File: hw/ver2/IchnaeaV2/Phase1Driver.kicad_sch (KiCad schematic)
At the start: 21 parts, among them Q2 MCAC80N10Y, Q3 MCAC80N10Y, Q4 MCAC80N10Y, Q5 MCAC80N10Y, U2 HIP2210

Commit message: Trying to optimize the high power loop area
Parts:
- renumbered C6 to C18, C7 to C19, C8 to C20, C9 to C21, C10 to C22, C11 to C23, C42 to C44, C48 to C50, C54 to C56, C60 to C62, D2 to D4, L1 to L3, Q2 to Q10, Q3 to Q11, Q4 to Q12, Q5 to Q13, R4 to R12, R5 to R13, R6 to R14, R7 to R15, U2 to U4
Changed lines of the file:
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@@
 		(on_board yes)
 		(dnp no)
-		(property "Reference" "R5"
+		(property "Reference" "R13"
 			(at 123.19 100.584 90)
 			(effects
@@
 		(on_board yes)
 		(dnp no)
-		(property "Reference" "C9"
+		(property "Reference" "C21"
 			(at 191.77 71.1199 0)
 			(effects
@@
 		(dnp no)
 		(fields_autoplaced yes)
-		(property "Reference" "C48"
+		(property "Reference" "C50"
 			(at 242.57 100.3299 0)
 			(effects
@@
 		(on_board yes)
 		(dnp no)
-		(property "Reference" "L1"
+		(property "Reference" "L3"
 			(at 203.2 92.456 90)
 			(effects
@@
 		(on_board yes)
 		(dnp no)
-		(property "Reference" "C6"
+		(property "Reference" "C18"
 			(at 87.63 95.2499 0)
 			(effects
@@
 		(dnp no)
 		(fields_autoplaced yes)
-		(property "Reference" "#PWR068"
+		(property "Reference" "#PWR070"
 			(at 227.33 111.76 0)
 			(effects
@@
 		(dnp no)
 		(fields_autoplaced yes)
-		(property "Reference" "#PWR045"
+		(property "Reference" "#PWR053"
 			(at 127 113.03 0)
 			(effects
@@
 		(dnp no)
 		(fields_autoplaced yes)
-		(property "Reference" "#PWR086"
+		(property "Reference" "#PWR088"
 			(at 261.62 111.76 0)
 			(effects
@@
 		(dnp no)
 		(fields_autoplaced yes)
-		(property "Reference" "R7"
+		(property "Reference" "R15"
 			(at 207.01 76.1999 0)
 			(effects
@@
 		(on_board yes)
 		(dnp no)
-		(property "Reference" "Q3"
+		(property "Reference" "Q11"
 			(at 153.924 109.22 0)
 			(effects
@@
 		(dnp no)
 		(fields_autoplaced yes)
-		(property "Reference" "C42"
+		(property "Reference" "C44"
 			(at 231.14 100.3299 0)
 			(effects
@@
 		(on_board yes)
 		(dnp no)
-		(property "Reference" "R4"
+		(property "Reference" "R12"
 			(at 111.76 86.868 90)
 			(effects
@@
 		(on_board yes)
 		(dnp no)
-		(property "Reference" "Q2"
+		(property "Reference" "Q10"
 			(at 155.956 79.502 0)
 			(effects
@@
 		(dnp no)
 		(fields_autoplaced yes)
-		(property "Reference" "C11"
+		(property "Reference" "C23"
 			(at 219.71 100.3299 0)
 			(effects
@@
 		(on_board yes)
 		(dnp no)
-		(property "Reference" "C8"
+		(property "Reference" "C20"
 			(at 145.796 84.328 0)
 			(effects
@@
 		(dnp no)
 		(fields_autoplaced yes)
-		(property "Reference" "#PWR080"
+		(property "Reference" "#PWR082"
 			(at 250.19 111.76 0)
 			(effects
@@
 		(dnp no)
 		(fields_autoplaced yes)
-		(property "Reference" "C10"
+		(property "Reference" "C22"
 			(at 208.28 66.0399 0)
 			(effects
@@
 		(dnp no)
 		(fields_autoplaced yes)
-		(property "Reference" "#PWR047"
+		(property "Reference" "#PWR055"
 			(at 215.9 111.76 0)
 			(effects
@@
 		(on_board yes)
 		(dnp no)
-		(property "Reference" "C7"
+		(property "Reference" "C19"
 			(at 101.6 95.2499 0)
 			(effects
@@
 		(on_board yes)
 		(dnp no)
-		(property "Reference" "Q4"
+		(property "Reference" "Q12"
 			(at 168.656 79.756 0)
 			(effects
@@
 		(dnp no)
 		(fields_autoplaced yes)
-		(property "Reference" "R6"
+		(property "Reference" "R14"
 			(at 190.5 76.2 90)
 			(effects
@@
 		(dnp no)
 		(fields_autoplaced yes)
-		(property "Reference" "#PWR074"
+		(property "Reference" "#PWR076"
 			(at 238.76 111.76 0)
 			(effects
@@
 		(on_board yes)
 		(dnp no)
-		(property "Reference" "Q5"
+		(property "Reference" "Q13"
 			(at 168.148 109.22 0)
 			(effects
@@
 		(on_board yes)
 		(dnp no)
-		(property "Reference" "D2"
+		(property "Reference" "D4"
 			(at 114.3 95.2499 90)
 			(effects
@@
 		(dnp no)
 		(fields_autoplaced yes)
-		(property "Reference" "C54"
+		(property "Reference" "C56"
 			(at 254 100.3299 0)
 			(effects
@@
 		(dnp no)
 		(fields_autoplaced yes)
-		(property "Reference" "#PWR044"
+		(property "Reference" "#PWR052"
 			(at 105.41 109.22 0)
 			(effects
@@
 		(dnp no)
 		(fields_autoplaced yes)
-		(property "Reference" "#PWR046"
+		(property "Reference" "#PWR054"
 			(at 162.56 113.03 0)
 			(effects
@@
 		(dnp no)
 		(fields_autoplaced yes)
-		(property "Reference" "C60"
+		(property "Reference" "C62"
 			(at 265.43 100.3299 0)
 			(effects
@@
 		(dnp no)
 		(fields_autoplaced yes)
-		(property "Reference" "U2"
+		(property "Reference" "U4"
 			(at 135.89 78.74 0)
 			(effects

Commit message: Trying to further compress power loop area
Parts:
- renumbered C22 to C10, C23 to C11, C44 to C42, C50 to C48, C56 to C54, C18 to C6, C62 to C60, C19 to C7, C20 to C8, C21 to C9, D4 to D2, L3 to L1, Q10 to Q2, Q11 to Q3, Q12 to Q4, Q13 to Q5, R12 to R4, R13 to R5, R14 to R6, R15 to R7, U4 to U2

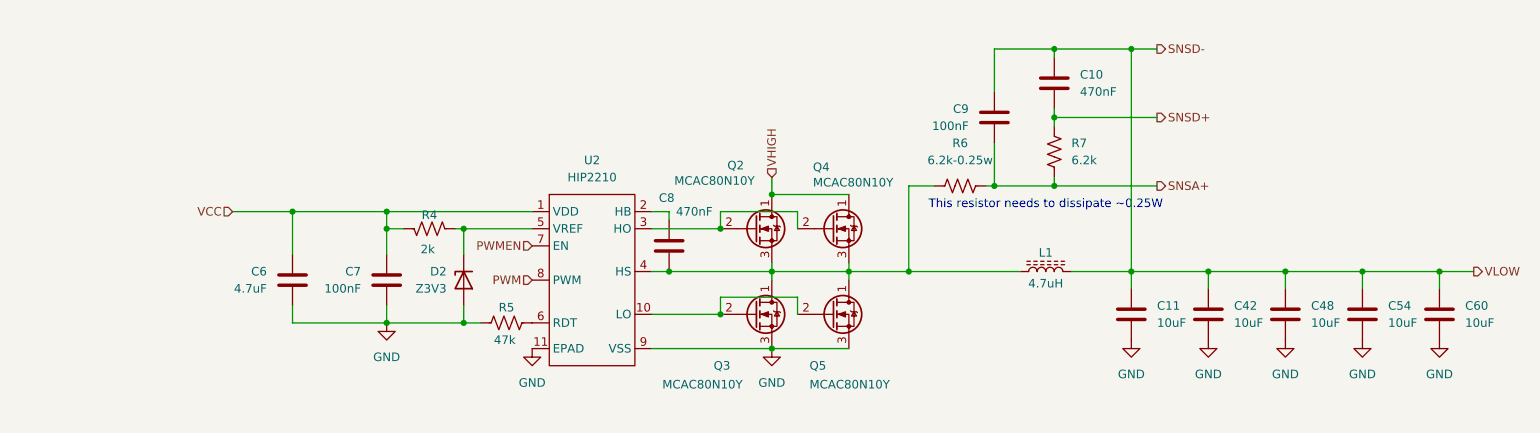
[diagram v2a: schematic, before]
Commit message: Not quite happy with the power stage just yet.
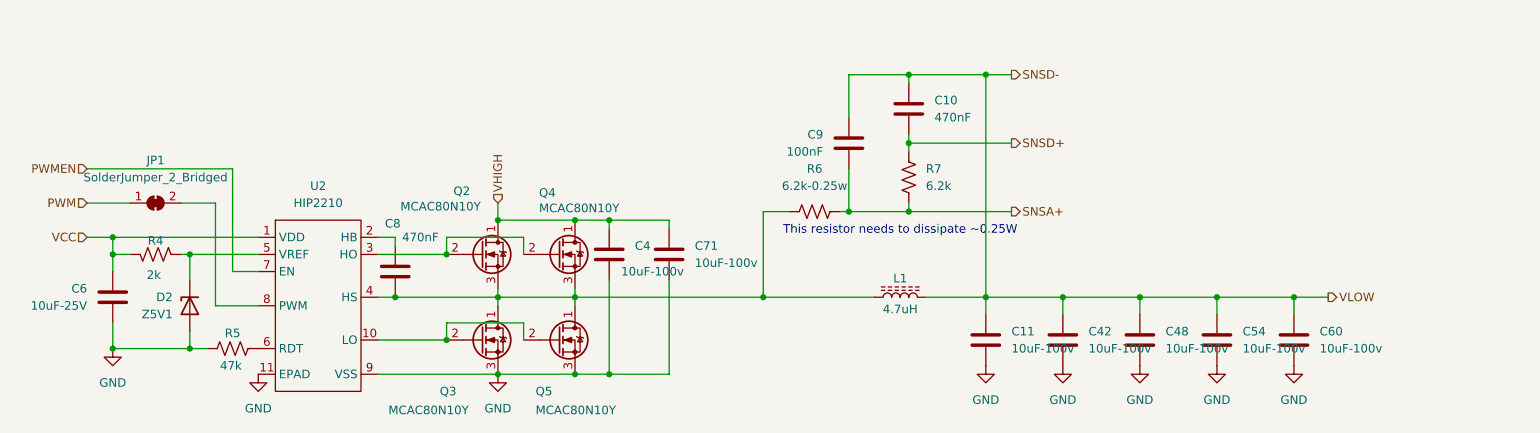
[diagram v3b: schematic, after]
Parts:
- removed C7: 100nF, Capacitor_SMD:C_0603_1608Metric, symbol Device:C
- added C4, C71: 10uF-100v, Capacitor_SMD:C_1210_3225Metric_Pad1.33x2.70mm_HandSolder, symbol Device:C
- added JP1: SolderJumper_2_Bridged, Jumper:SolderJumper-2_P1.3mm_Bridged_Pad1.0x1.5mm, symbol Jumper:SolderJumper_2_Bridged
- C11, C42, C48, C54, C60: value 10uF -> 10uF-100v
- C6: value 4.7uF -> 10uF-25V; LCSC C19666 -> C96446
- D2: value Z3V3 -> Z5V1; LCSC C5353025 -> C2903912
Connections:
- net GND: now also C4.2, C71.2
- net PWM: now also JP1.1 (A); no longer U2.8 (PWM)
- net VHIGH: now also C4.1, C71.1
- new net: JP1.2 (B), U2.8 (PWM)
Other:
- moved on the sheet: C10, C11, C42, C48, C54, C6, C60, C8, C9, D2, L1, Q2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

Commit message: Sync work to main PC
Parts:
- removed D2: Z5V1, Diode_SMD:D_SOD-123, symbol Device:D_Zener
- removed JP1: SolderJumper_2_Bridged, Jumper:SolderJumper-2_P1.3mm_Bridged_Pad1.0x1.5mm, symbol Jumper:SolderJumper_2_Bridged
- added R74: 0, Resistor_SMD:R_0603_1608Metric, symbol Device:R_US
- added R75: 10k, Resistor_SMD:R_0603_1608Metric, symbol Device:R_US
- added R76: 6.2k, Resistor_SMD:R_0603_1608Metric, symbol Device:R_US
- R4: value 2k -> 0; LCSC (none) -> C21189
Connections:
- net GND: now also R76.2
- net PWM: now also R74.2
- net PWMEN: now also R4.2; no longer U2.7 (EN)
- net SNSD-: now also L1.1; no longer L1.2
- net VCC: now also R75.1; no longer R4.2
- net at C8.2, Q2.3 (S), Q3.1 (D)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: now also L1.2; no longer L1.1
- net at U2.5 (VREF): now also R75.2, R76.1; no longer R4.1
- net at U2.8 (PWM): now also R74.1
- new net: R4.1, U2.7 (EN)
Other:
- moved on the sheet: L1

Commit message: More power stage layout
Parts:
- added TP10, TP11, TP12, TP13, TP6, TP7, TP8, TP9: TestPoint, TestPoint:TestPoint_Pad_D1.0mm, symbol Connector:TestPoint
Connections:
- net GND: now also TP10.1
- net PWM: now also TP7.1
- net PWMEN: now also TP6.1
- net SNSA+: now also TP13.1
- net SNSD+: now also TP12.1
- net SNSD-: now also TP11.1
- net at Q3.2 (G), Q5.2 (G), U2.10 (LO): now also TP8.1
- net at Q2.2 (G), Q4.2 (G), U2.3 (HO): now also TP9.1

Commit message: Partially work through the V1 notes. Start adding some of the control stage circuitry.
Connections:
- net GND: now also TP12.1
- net SNSA+: no longer TP13.1
- net SNSD+: no longer TP12.1
- net at C8.2, L1.2, Q2.3 (S)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: now also TP13.1
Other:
- moved on the sheet: TP11, TP12, TP13
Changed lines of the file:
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@@
 	)
 	(junction
-		(at 217.17 99.06)
+		(at 161.29 86.36)
 		(diameter 0)
 		(color 0 0 0 0)
 	)
 	(junction
-		(at 76.2 92.71)
+		(at 217.17 99.06)
 		(diameter 0)
 		(color 0 0 0 0)
 	)
 	(junction
-		(at 195.58 66.04)
+		(at 76.2 92.71)
 		(diameter 0)
 		(color 0 0 0 0)
@@
 	)
 	(junction
-		(at 195.58 76.2)
-		(diameter 0)
-		(color 0 0 0 0)
-	)
-	(junction
 		(at 205.74 99.06)
 		(diameter 0)
@@
 	)
 	(junction
-		(at 195.58 86.36)
-		(diameter 0)
-		(color 0 0 0 0)
-	)
-	(junction
 		(at 194.31 99.06)
 		(diameter 0)
@@
 	(wire
 		(pts
-			(xy 195.58 86.36) (xy 198.12 86.36)
-		)
-		(stroke
-			(width 0)
-			(type default)
-		)
-	)
-	(wire
-		(pts
 			(xy 111.76 113.03) (xy 113.03 113.03)
 		)
@@
 	(wire
 		(pts
-			(xy 182.88 86.36) (xy 195.58 86.36)
+			(xy 182.88 86.36) (xy 198.12 86.36)
 		)
 		(stroke
@@
 	(wire
 		(pts
-			(xy 195.58 73.66) (xy 195.58 76.2)
-		)
-		(stroke
-			(width 0)
-			(type default)
-		)
-	)
-	(wire
-		(pts
 			(xy 125.73 90.17) (xy 114.3 90.17)
 		)
@@
 	(wire
 		(pts
-			(xy 195.58 66.04) (xy 194.31 66.04)
+			(xy 194.31 66.04) (xy 198.12 66.04)
 		)
 		(stroke
@@
 	(wire
 		(pts
-			(xy 198.12 66.04) (xy 195.58 66.04)
-		)
-		(stroke
-			(width 0)
-			(type default)
-		)
-	)
-	(wire
-		(pts
 			(xy 185.42 99.06) (xy 194.31 99.06)
 		)
@@
 	(wire
 		(pts
-			(xy 195.58 76.2) (xy 198.12 76.2)
-		)
-		(stroke
-			(width 0)
-			(type default)
-		)
-	)
-	(wire
-		(pts
 			(xy 172.72 86.36) (xy 173.99 86.36)
 		)
@@
 	(wire
 		(pts
-			(xy 182.88 76.2) (xy 195.58 76.2)
+			(xy 182.88 76.2) (xy 198.12 76.2)
 		)
 		(stroke
@@
 	(wire
 		(pts
-			(xy 195.58 83.82) (xy 195.58 86.36)
-		)
-		(stroke
-			(width 0)
-			(type default)
-		)
-	)
-	(wire
-		(pts
 			(xy 76.2 92.71) (xy 86.36 92.71)
 		)
@@
 		)
 	)
-	(wire
-		(pts
-			(xy 195.58 63.5) (xy 195.58 66.04)
-		)
-		(stroke
-			(width 0)
-			(type default)
-		)
-	)
 	(text "This resistor needs to dissipate ~0.25W"
 		(exclude_from_sim no)
@@
 	(symbol
 		(lib_id "Connector:TestPoint")
-		(at 195.58 83.82 270)
+		(at 161.29 86.36 0)
 		(unit 1)
 		(exclude_from_sim no)
@@
 		(dnp no)
 		(property "Reference" "TP13"
-			(at 201.93 83.82 90)
+			(at 161.29 80.01 90)
 			(effects
 				(font
@@
 		)
 		(property "Value" "TestPoint"
-			(at 198.882 86.36 90)
+			(at 163.83 83.058 90)
 			(effects
 				(font
@@
 		)
 		(property "Footprint" "TestPoint:TestPoint_Pad_D1.0mm"
-			(at 195.58 88.9 0)
+			(at 166.37 86.36 0)
 			(effects
 				(font
@@
 		)
 		(property "Datasheet" "~"
-			(at 195.58 88.9 0)
+			(at 166.37 86.36 0)
 			(effects
 				(font
@@
 		)
 		(property "Description" "test point"
-			(at 195.58 83.82 0)
+			(at 161.29 86.36 0)
 			(effects
 				(font
@@
 	(symbol
 		(lib_id "Connector:TestPoint")
-		(at 195.58 63.5 270)
+		(at 194.31 66.04 0)
 		(unit 1)
 		(exclude_from_sim no)
@@
 		(dnp no)
 		(property "Reference" "TP11"
-			(at 201.93 63.5 90)
+			(at 194.31 59.69 90)
 			(effects
 				(font
@@
 		)
 		(property "Value" "TestPoint"
-			(at 198.882 66.04 90)
+			(at 196.85 62.738 90)
 			(effects
 				(font
@@
 		)
 		(property "Footprint" "TestPoint:TestPoint_Pad_D1.0mm"
-			(at 195.58 68.58 0)
+			(at 199.39 66.04 0)
 			(effects
 				(font
@@
 		)
 		(property "Datasheet" "~"
-			(at 195.58 68.58 0)
+			(at 199.39 66.04 0)
 			(effects
 				(font
@@
 		)
 		(property "Description" "test point"
-			(at 195.58 63.5 0)
+			(at 194.31 66.04 0)
 			(effects
 				(font
@@
 	(symbol
 		(lib_id "power:GND")
+		(at 158.75 86.36 0)
+		(unit 1)
+		(exclude_from_sim no)
+		(in_bom yes)
+		(on_board yes)
+		(dnp no)
+		(fields_autoplaced yes)
+		(property "Reference" "#PWR0139"
+			(at 158.75 92.71 0)
+			(effects
+				(font
+					(size 1.27 1.27)
+				)
+				(hide yes)
+			)
+		)
+		(property "Value" "GND"
+			(at 158.75 91.44 0)
+			(effects
+				(font
+					(size 1.27 1.27)
+				)
+			)
+		)
+		(property "Footprint" ""
+			(at 158.75 86.36 0)
+			(effects
+				(font
+					(size 1.27 1.27)
+				)
+				(hide yes)
+			)
+		)
+		(property "Datasheet" ""
+			(at 158.75 86.36 0)
+			(effects
+				(font
+					(size 1.27 1.27)
+				)
+				(hide yes)
+			)
+		)
+		(property "Description" "Power symbol creates a global label with name \"GND\" , ground"
+			(at 158.75 86.36 0)
+			(effects
+				(font
+					(size 1.27 1.27)
+				)
+				(hide yes)
+			)
+		)
+		(pin "1"
+		)
+		(instances
+			(project "IchnaeaV2"
+				(path "/93408532-1ffa-463d-873c-16289d2b7987/31a930eb-86fc-490d-aa2b-31b72c4dd29d/171364aa-6f2d-4723-9ce2-aacc140a6e7a"
+					(reference "#PWR0139")
+					(unit 1)
+				)
+			)
+		)
+	)
+	(symbol
+		(lib_id "power:GND")
 		(at 194.31 109.22 0)
 		(unit 1)
@@
 	(symbol
 		(lib_id "Connector:TestPoint")
-		(at 195.58 73.66 270)
+		(at 158.75 86.36 0)
 		(unit 1)
 		(exclude_from_sim no)
@@
 		(dnp no)
 		(property "Reference" "TP12"
-			(at 201.93 73.66 90)
+			(at 158.75 80.01 90)
 			(effects
 				(font
@@
 		)
 		(property "Value" "TestPoint"
-			(at 198.882 76.2 90)
+			(at 161.29 83.058 90)
 			(effects
 				(font
@@
 		)
 		(property "Footprint" "TestPoint:TestPoint_Pad_D1.0mm"
-			(at 195.58 78.74 0)
+			(at 163.83 86.36 0)
 			(effects
 				(font
@@
 		)
 		(property "Datasheet" "~"
-			(at 195.58 78.74 0)
+			(at 163.83 86.36 0)
 			(effects
 				(font
@@
 		)
 		(property "Description" "test point"
-			(at 195.58 73.66 0)
+			(at 158.75 86.36 0)
 			(effects
 				(font
